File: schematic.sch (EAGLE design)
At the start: 14 parts, among them J1 FTDI_DEVICE, U1 ATMEGA328P_TQFP, U2 GY-521MPU6050

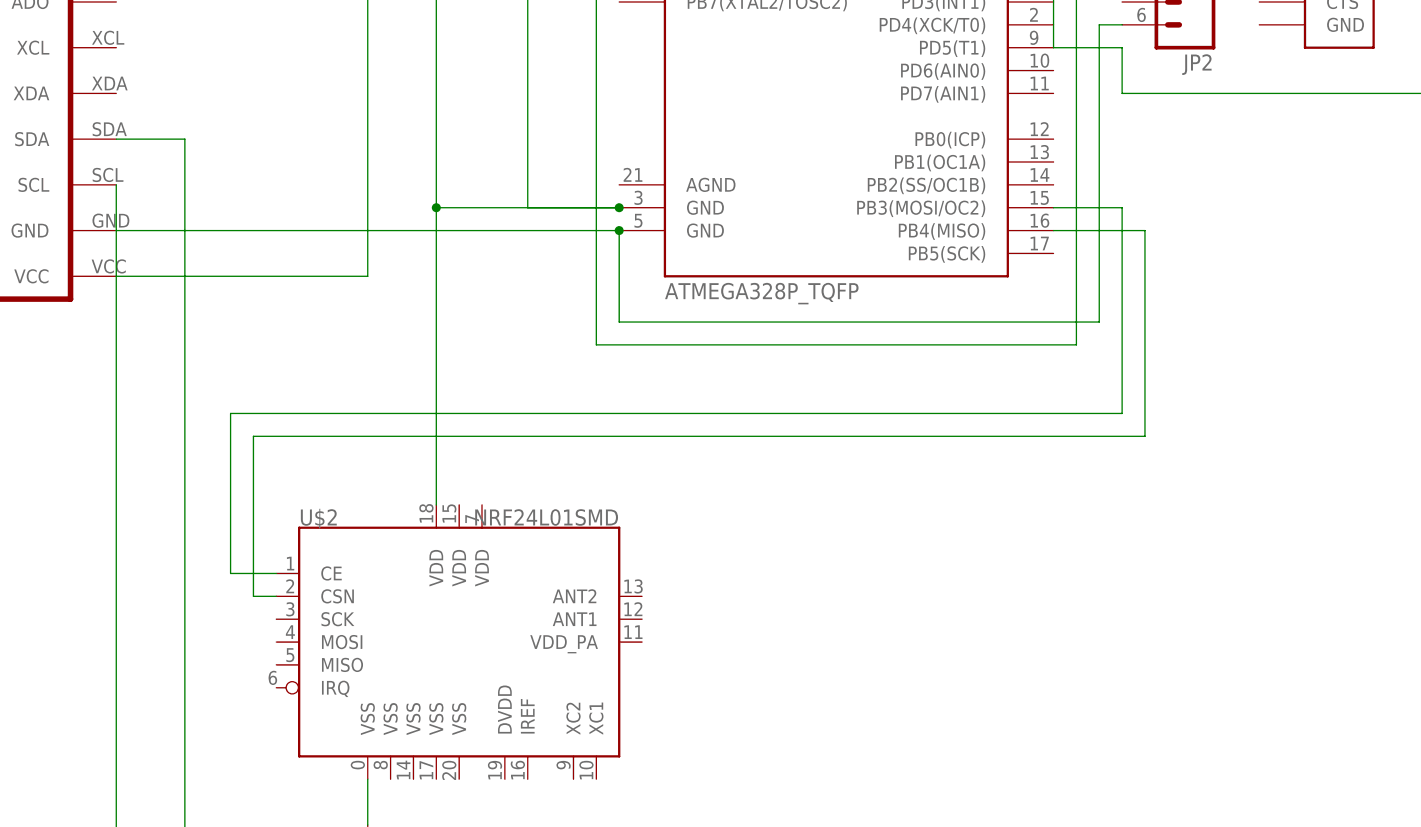
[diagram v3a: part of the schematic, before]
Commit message: Updated connections to radio module
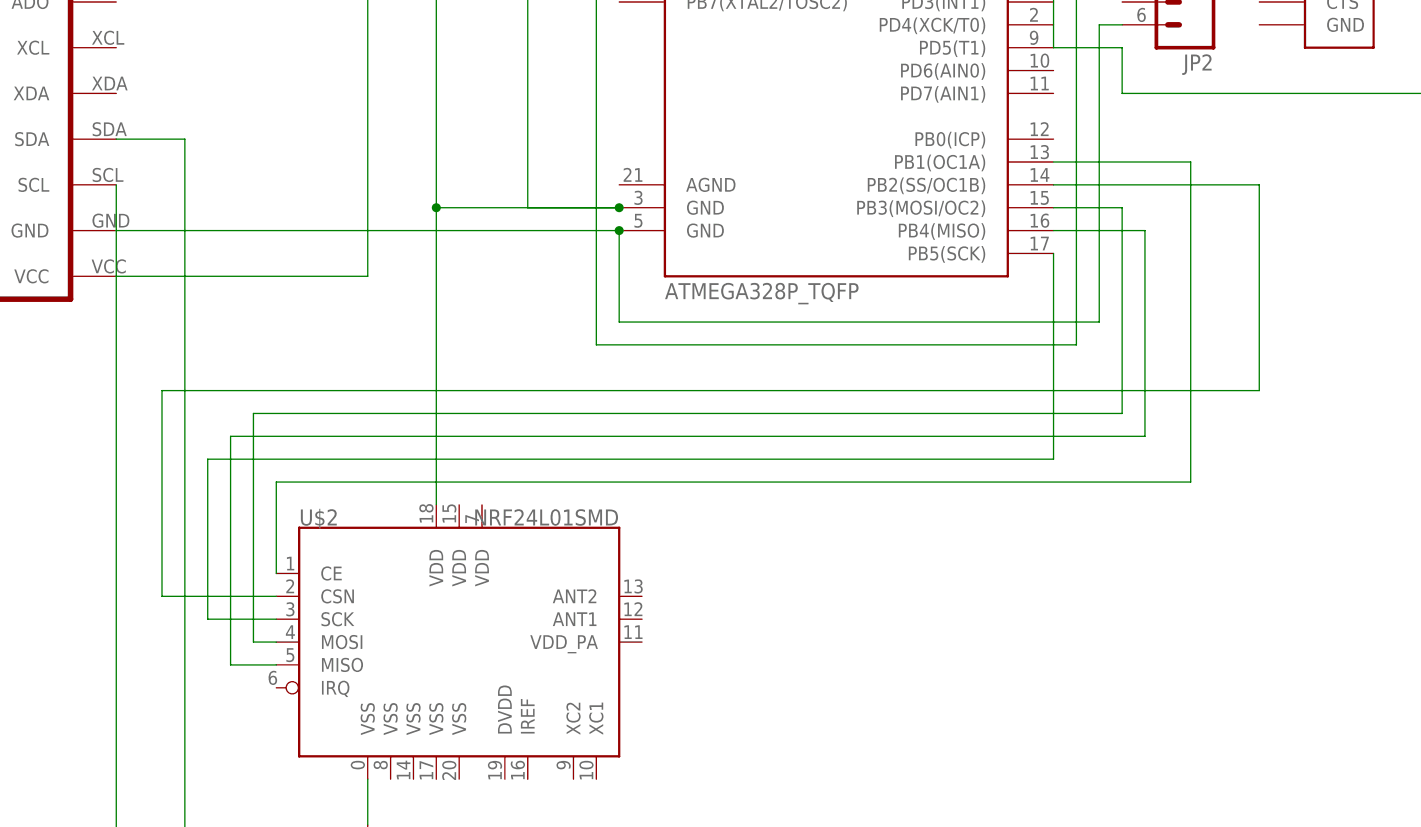
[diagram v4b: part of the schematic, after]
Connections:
- new net N$20: U$2.SCK, U1.PB5(SCK)
- new net N$21: U$2.CE, U1.PB1(OC1A)
- new net N$22: U$2.CSN, U1.PB2(SS/OC1B)
- net N$14: now also U$2.MOSI; no longer U$2.CE
- net N$15: now also U$2.MISO; no longer U$2.CSN
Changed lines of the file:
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@@
 <wire x1="86.36" y1="15.24" x2="93.98" y2="15.24" width="0.1524" layer="91"/>
 <wire x1="93.98" y1="15.24" x2="93.98" y2="-7.62" width="0.1524" layer="91"/>
-<wire x1="93.98" y1="-7.62" x2="-5.08" y2="-7.62" width="0.1524" layer="91"/>
-<pinref part="U$2" gate="G$1" pin="CE"/>
-<wire x1="-5.08" y1="-7.62" x2="-5.08" y2="-25.4" width="0.1524" layer="91"/>
-<wire x1="-5.08" y1="-25.4" x2="0" y2="-25.4" width="0.1524" layer="91"/>
+<wire x1="93.98" y1="-7.62" x2="-2.54" y2="-7.62" width="0.1524" layer="91"/>
+<wire x1="-2.54" y1="-7.62" x2="-2.54" y2="-33.02" width="0.1524" layer="91"/>
+<pinref part="U$2" gate="G$1" pin="MOSI"/>
+<wire x1="-2.54" y1="-33.02" x2="0" y2="-33.02" width="0.1524" layer="91"/>
 </segment>
 </net>
@@
 <wire x1="86.36" y1="12.7" x2="96.52" y2="12.7" width="0.1524" layer="91"/>
 <wire x1="96.52" y1="12.7" x2="96.52" y2="-10.16" width="0.1524" layer="91"/>
-<wire x1="96.52" y1="-10.16" x2="-2.54" y2="-10.16" width="0.1524" layer="91"/>
-<wire x1="-2.54" y1="-10.16" x2="-2.54" y2="-27.94" width="0.1524" layer="91"/>
-<pinref part="U$2" gate="G$1" pin="CSN"/>
-<wire x1="-2.54" y1="-27.94" x2="0" y2="-27.94" width="0.1524" layer="91"/>
+<wire x1="96.52" y1="-10.16" x2="-5.08" y2="-10.16" width="0.1524" layer="91"/>
+<wire x1="-5.08" y1="-10.16" x2="-5.08" y2="-35.56" width="0.1524" layer="91"/>
+<pinref part="U$2" gate="G$1" pin="MISO"/>
+<wire x1="-5.08" y1="-35.56" x2="0" y2="-35.56" width="0.1524" layer="91"/>
 </segment>
 </net>
@@
 </segment>
 </net>
+<net name="N$20" class="0">
+<segment>
+<pinref part="U1" gate="U$1" pin="PB5(SCK)"/>
+<wire x1="86.36" y1="10.16" x2="86.36" y2="-12.7" width="0.1524" layer="91"/>
+<wire x1="86.36" y1="-12.7" x2="-7.62" y2="-12.7" width="0.1524" layer="91"/>
+<wire x1="-7.62" y1="-12.7" x2="-7.62" y2="-30.48" width="0.1524" layer="91"/>
+<pinref part="U$2" gate="G$1" pin="SCK"/>
+<wire x1="-7.62" y1="-30.48" x2="0" y2="-30.48" width="0.1524" layer="91"/>
+</segment>
+</net>
+<net name="N$21" class="0">
+<segment>
+<pinref part="U$2" gate="G$1" pin="CE"/>
+<wire x1="0" y1="-25.4" x2="0" y2="-15.24" width="0.1524" layer="91"/>
+<wire x1="0" y1="-15.24" x2="101.6" y2="-15.24" width="0.1524" layer="91"/>
+<wire x1="101.6" y1="-15.24" x2="101.6" y2="20.32" width="0.1524" layer="91"/>
+<pinref part="U1" gate="U$1" pin="PB1(OC1A)"/>
+<wire x1="101.6" y1="20.32" x2="86.36" y2="20.32" width="0.1524" layer="91"/>
+</segment>
+</net>
+<net name="N$22" class="0">
+<segment>
+<pinref part="U$2" gate="G$1" pin="CSN"/>
+<wire x1="0" y1="-27.94" x2="-12.7" y2="-27.94" width="0.1524" layer="91"/>
+<wire x1="-12.7" y1="-27.94" x2="-12.7" y2="-5.08" width="0.1524" layer="91"/>
+<wire x1="-12.7" y1="-5.08" x2="109.22" y2="-5.08" width="0.1524" layer="91"/>
+<pinref part="U1" gate="U$1" pin="PB2(SS/OC1B)"/>
+<wire x1="109.22" y1="-5.08" x2="109.22" y2="17.78" width="0.1524" layer="91"/>
+<wire x1="109.22" y1="17.78" x2="86.36" y2="17.78" width="0.1524" layer="91"/>
+</segment>
+</net>

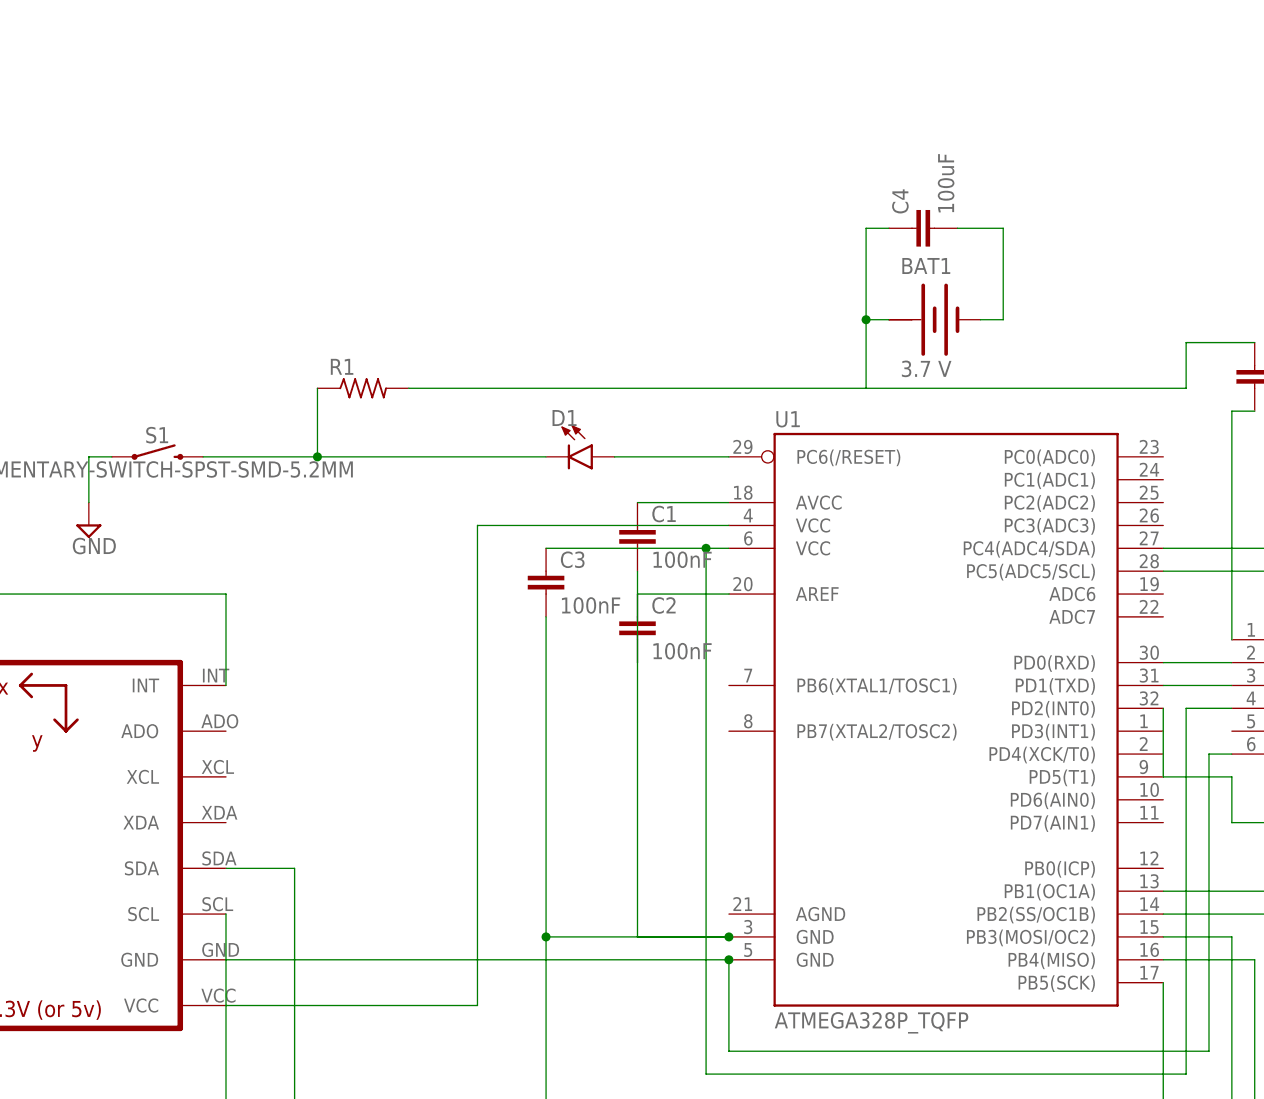
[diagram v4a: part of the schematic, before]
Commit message: Added buck-boost converter
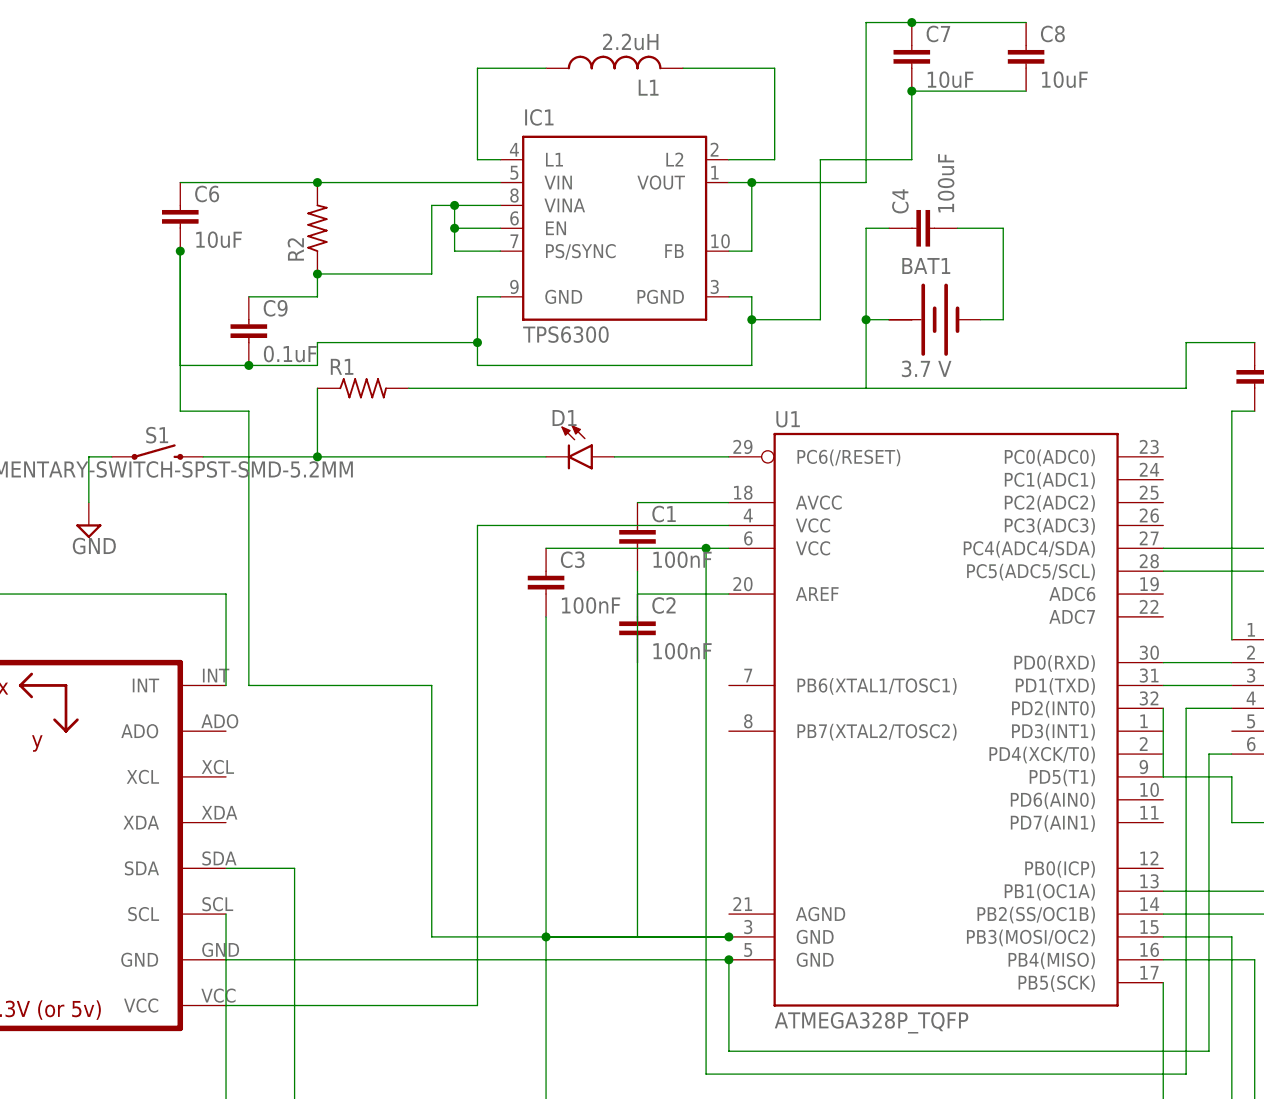
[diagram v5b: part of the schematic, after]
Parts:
- added C6, C7, C8: 10uF, rcl:C-EUC0603
- added C9: 0.1uF, rcl:C-EUC0603
- added IC1: TPS6300, texas:TPS6300
- added L1: 2.2uH, rcl:L-US0204/5
- added R2: (no value), rcl:R-US_R0603
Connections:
- removed net N$6: C1.2, C2.2, C3.2, U$2.VDD@18, U1.GND@3
- new net N$23: IC1G$1.L1, L1.1
- new net N$24: IC1G$1.L2, L1.2
- new net N$25: C7.1, C8.1, IC1G$1.FB, IC1G$1.VOUT
- new net N$27: C6.1, IC1G$1.VIN, R2.2
- new net N$28: C9.1, IC1G$1.EN, IC1G$1.PS/SYNC, IC1G$1.VINA, R2.1
- new net N$29: C1.2, C2.2, C3.2, C6.2, C7.2, C8.2, C9.2, IC1G$1.GND, IC1G$1.PGND, U$2.VDD@18, U1.GND@3
